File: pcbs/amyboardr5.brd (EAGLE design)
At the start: 106.1 x 47.5 mm, 144 parts, among them J1 52601-G10-8LF, Q2 S8050, Q5 S8050, U1 PCM9211PT, U15 H11L1SR2M, U16 SPX3819, U2 ESP32­S2­SOLO, U3 SPX3819, U4 TL074CD, U6 HX3608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

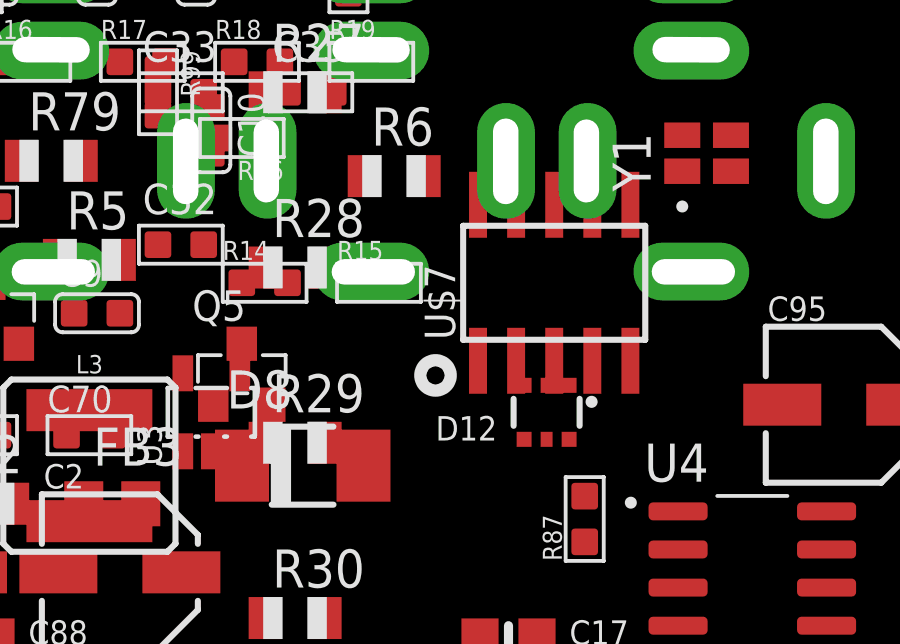
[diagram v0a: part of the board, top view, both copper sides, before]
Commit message: CVOUT fixes
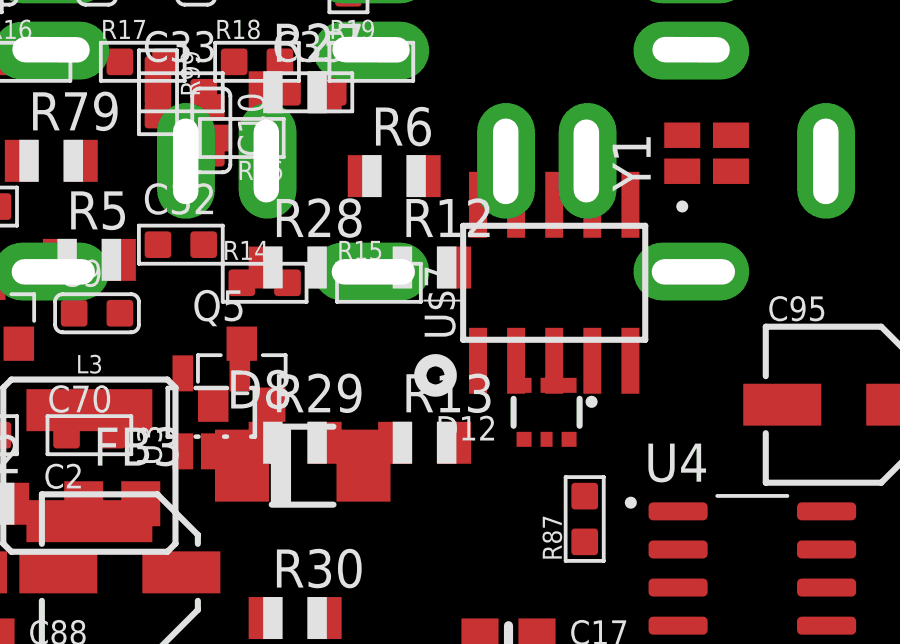
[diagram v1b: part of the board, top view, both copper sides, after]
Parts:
- added R12, R13: 10K, adafruit:R0805
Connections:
- net +3V3: now also R12.1, R13.1
- net N$31: now also R13.2
- net N$33: now also R12.2
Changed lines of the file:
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@@
 <attribute name="VALUE" x="39.116" y="31.1785" size="1.016" layer="27" ratio="12"/>
+</element>
+<element name="R12" library="adafruit" package="R0805" value="10K" x="44.196" y="27.178" smashed="yes">
+<attribute name="NAME" x="43.434" y="28.194" size="1.27" layer="25"/>
+<attribute name="VALUE" x="43.434" y="24.892" size="1.27" layer="27"/>
+</element>
+<element name="R13" library="adafruit" package="R0805" value="10K" x="44.196" y="21.336" smashed="yes">
+<attribute name="NAME" x="43.434" y="22.352" size="1.27" layer="25"/>
+<attribute name="VALUE" x="43.434" y="19.05" size="1.27" layer="27"/>
 </element>
 </elements>
@@
 <contactref element="C107" pad="1"/>
 <contactref element="U16" pad="5"/>
-<wire x1="4.572" y1="35.306" x2="32.02" y2="27.432" width="0" layer="19" extent="1-1"/>
-<wire x1="3.81" y1="25.974" x2="4.572" y2="35.306" width="0" layer="19" extent="1-1"/>
-<wire x1="9.144" y1="20.132" x2="3.81" y2="25.974" width="0" layer="19" extent="1-1"/>
+<contactref element="R12" pad="1"/>
+<contactref element="R13" pad="1"/>
+<wire x1="95.62" y1="43.152" x2="101.026" y2="42.926" width="0" layer="19" extent="1-1"/>
+<wire x1="95.62" y1="44.152" x2="95.62" y2="43.152" width="0" layer="19" extent="1-1"/>
+<wire x1="91.69" y1="45.582" x2="95.62" y2="44.152" width="0" layer="19" extent="1-1"/>
+<wire x1="93.19" y1="37.222" x2="95.62" y2="43.152" width="0" layer="19" extent="1-1"/>
+<wire x1="93.98" y1="26.67" x2="93.19" y2="37.222" width="0" layer="19" extent="1-1"/>
+<wire x1="99.38" y1="28.2241" x2="93.98" y2="26.67" width="0" layer="19" extent="1-1"/>
+<wire x1="106.172" y1="23.876" x2="99.38" y2="28.2241" width="0" layer="19" extent="1-1"/>
+<wire x1="101.6" y1="19.304" x2="106.172" y2="23.876" width="0" layer="19" extent="1-1"/>
+<wire x1="96.604" y1="14.478" x2="101.6" y2="19.304" width="0" layer="19" extent="1-1"/>
+<wire x1="94.506" y1="16.256" x2="96.604" y2="14.478" width="0" layer="19" extent="1-1"/>
+<wire x1="86.106" y1="3.81" x2="96.604" y2="14.478" width="0" layer="19" extent="1-1"/>
+<wire x1="81.026" y1="6.35" x2="86.106" y2="3.81" width="0" layer="19" extent="1-1"/>
+<wire x1="69.215" y1="5.801" x2="81.026" y2="6.35" width="0" layer="19" extent="1-1"/>
+<wire x1="69.215" y1="7.750996875" x2="69.215" y2="5.801" width="0" layer="19" extent="1-1"/>
+<wire x1="63.373" y1="7.751" x2="69.215" y2="7.750996875" width="0" layer="19" extent="1-1"/>
+<wire x1="63.373" y1="3.201003125" x2="63.373" y2="7.751" width="0" layer="19" extent="1-1"/>
+<wire x1="71.392" y1="16.256" x2="69.215" y2="7.750996875" width="0" layer="19" extent="1-1"/>
+<wire x1="74.422" y1="21.082" x2="71.392" y2="16.256" width="0" layer="19" extent="1-1"/>
+<wire x1="67.582" y1="22.606" x2="74.422" y2="21.082" width="0" layer="19" extent="1-1"/>
+<wire x1="60.216" y1="22.606" x2="67.582" y2="22.606" width="0" layer="19" extent="1-1"/>
+<wire x1="61.214" y1="30.988" x2="60.216" y2="22.606" width="0" layer="19" extent="1-1"/>
+<wire x1="49.53" y1="18.034" x2="60.216" y2="22.606" width="0" layer="19" extent="1-1"/>
+<wire x1="47.51" y1="21.452" x2="49.53" y2="18.034" width="0" layer="19" extent="1-1"/>
+<wire x1="66.434" y1="41.582" x2="61.214" y2="30.988" width="0" layer="19" extent="1-1"/>
+<wire x1="37.338" y1="31.496" x2="47.51" y2="21.452" width="0" layer="19" extent="1-1"/>
+<wire x1="35.306" y1="32.258" x2="37.338" y2="31.496" width="0" layer="19" extent="1-1"/>
+<wire x1="32.02" y1="27.432" x2="35.306" y2="32.258" width="0" layer="19" extent="1-1"/>
+<wire x1="41.656" y1="36.322" x2="37.338" y2="31.496" width="0" layer="19" extent="1-1"/>
+<wire x1="38.608" y1="40.132" x2="41.656" y2="36.322" width="0" layer="19" extent="1-1"/>
+<wire x1="25.4" y1="23.434" x2="32.02" y2="27.432" width="0" layer="19" extent="1-1"/>
+<wire x1="21.1" y1="22.098" x2="25.4" y2="23.434" width="0" layer="19" extent="1-1"/>
+<wire x1="29.906" y1="14.732" x2="25.4" y2="23.434" width="0" layer="19" extent="1-1"/>
+<wire x1="30.988" y1="10.922" x2="29.906" y2="14.732" width="0" layer="19" extent="1-1"/>
+<wire x1="10.43" y1="23.876" x2="21.1" y2="22.098" width="0" layer="19" extent="1-1"/>
+<wire x1="9.144" y1="20.132" x2="10.43" y2="23.876" width="0" layer="19" extent="1-1"/>
 <wire x1="9.398" y1="15.936" x2="9.144" y2="20.132" width="0" layer="19" extent="1-1"/>
 <wire x1="12.7" y1="13.97" x2="9.398" y2="15.936" width="0" layer="19" extent="1-1"/>
-<wire x1="30.988" y1="10.922" x2="12.7" y2="13.97" width="0" layer="19" extent="1-1"/>
+<wire x1="3.81" y1="25.974" x2="10.43" y2="23.876" width="0" layer="19" extent="1-1"/>
 <wire x1="3.71" y1="9.636" x2="9.398" y2="15.936" width="0" layer="19" extent="1-16"/>
-<wire x1="21.1" y1="22.098" x2="30.988" y2="10.922" width="0" layer="19" extent="1-1"/>
-<wire x1="25.4" y1="23.434" x2="21.1" y2="22.098" width="0" layer="19" extent="1-1"/>
-<wire x1="29.906" y1="14.732" x2="25.4" y2="23.434" width="0" layer="19" extent="1-1"/>
-<wire x1="35.306" y1="32.258" x2="25.4" y2="23.434" width="0" layer="19" extent="1-1"/>
-<wire x1="37.338" y1="31.496" x2="35.306" y2="32.258" width="0" layer="19" extent="1-1"/>
-<wire x1="41.656" y1="36.322" x2="37.338" y2="31.496" width="0" layer="19" extent="1-1"/>
-<wire x1="38.608" y1="40.132" x2="41.656" y2="36.322" width="0" layer="19" extent="1-1"/>
-<wire x1="47.51" y1="21.452" x2="37.338" y2="31.496" width="0" layer="19" extent="1-1"/>
-<wire x1="49.53" y1="18.034" x2="47.51" y2="21.452" width="0" layer="19" extent="1-1"/>
-<wire x1="60.216" y1="22.606" x2="49.53" y2="18.034" width="0" layer="19" extent="1-1"/>
-<wire x1="67.582" y1="22.606" x2="60.216" y2="22.606" width="0" layer="19" extent="1-1"/>
-<wire x1="74.422" y1="21.082" x2="67.582" y2="22.606" width="0" layer="19" extent="1-1"/>
-<wire x1="71.392" y1="16.256" x2="74.422" y2="21.082" width="0" layer="19" extent="1-1"/>
-<wire x1="61.214" y1="30.988" x2="60.216" y2="22.606" width="0" layer="19" extent="1-1"/>
-<wire x1="69.215" y1="7.750996875" x2="71.392" y2="16.256" width="0" layer="19" extent="1-1"/>
-<wire x1="69.215" y1="5.801" x2="69.215" y2="7.750996875" width="0" layer="19" extent="1-1"/>
-<wire x1="63.373" y1="7.751" x2="69.215" y2="7.750996875" width="0" layer="19" extent="1-1"/>
-<wire x1="63.373" y1="3.201003125" x2="63.373" y2="7.751" width="0" layer="19" extent="1-1"/>
-<wire x1="66.434" y1="41.582" x2="61.214" y2="30.988" width="0" layer="19" extent="1-1"/>
-<wire x1="81.026" y1="6.35" x2="69.215" y2="5.801" width="0" layer="19" extent="1-1"/>
-<wire x1="86.106" y1="3.81" x2="81.026" y2="6.35" width="0" layer="19" extent="1-1"/>
-<wire x1="96.604" y1="14.478" x2="86.106" y2="3.81" width="0" layer="19" extent="1-1"/>
-<wire x1="94.506" y1="16.256" x2="96.604" y2="14.478" width="0" layer="19" extent="1-1"/>
-<wire x1="101.6" y1="19.304" x2="96.604" y2="14.478" width="0" layer="19" extent="1-1"/>
-<wire x1="106.172" y1="23.876" x2="101.6" y2="19.304" width="0" layer="19" extent="1-1"/>
-<wire x1="99.38" y1="28.2241" x2="106.172" y2="23.876" width="0" layer="19" extent="1-1"/>
-<wire x1="93.98" y1="26.67" x2="99.38" y2="28.2241" width="0" layer="19" extent="1-1"/>
-<wire x1="93.19" y1="37.222" x2="93.98" y2="26.67" width="0" layer="19" extent="1-1"/>
-<wire x1="95.62" y1="43.152" x2="93.19" y2="37.222" width="0" layer="19" extent="1-1"/>
-<wire x1="95.62" y1="44.152" x2="95.62" y2="43.152" width="0" layer="19" extent="1-1"/>
-<wire x1="91.69" y1="45.582" x2="95.62" y2="44.152" width="0" layer="19" extent="1-1"/>
-<wire x1="101.026" y1="42.926" x2="95.62" y2="43.152" width="0" layer="19" extent="1-1"/>
-<wire x1="10.43" y1="23.876" x2="32.02" y2="27.432" width="0" layer="19" extent="1-1"/>
+<wire x1="4.572" y1="35.306" x2="3.81" y2="25.974" width="0" layer="19" extent="1-1"/>
+<wire x1="43.196" y1="21.336" x2="101.026" y2="42.926" width="0" layer="19" extent="1-1"/>
+<wire x1="43.196" y1="27.178" x2="43.196" y2="21.336" width="0" layer="19" extent="1-1"/>
 </signal>
 <signal name="DTR">
@@
 <contactref element="R11" pad="1"/>
 <contactref element="U4" pad="6"/>
-<wire x1="4.08" y1="16.256" x2="52.643" y2="12.7" width="0" layer="19" extent="1-1"/>
-<wire x1="4.08" y1="10.414" x2="4.08" y2="16.256" width="0" layer="19" extent="1-1"/>
+<contactref element="R13" pad="2"/>
+<wire x1="52.643" y1="12.7" x2="45.196" y2="21.336" width="0" layer="19" extent="1-1"/>
+<wire x1="4.08" y1="10.414" x2="52.643" y2="12.7" width="0" layer="19" extent="1-1"/>
+<wire x1="4.08" y1="16.256" x2="4.08" y2="10.414" width="0" layer="19" extent="1-1"/>
 </signal>
 <signal name="N$33">
 <contactref element="R22" pad="1"/>
 <contactref element="U4" pad="2"/>
+<contactref element="R12" pad="2"/>
+<wire x1="52.643" y1="17.78" x2="45.196" y2="27.178" width="0" layer="19" extent="1-1"/>
 <wire x1="4.08" y1="4.572" x2="52.643" y2="17.78" width="0" layer="19" extent="1-1"/>
 </signal>

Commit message: dans fixes
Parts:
- R5: value 10K -> 30K
- R6: value 15K -> 10K
- R8: value 30K -> 15K
- moved C10 324.9 mm to (-284.7, 76.5)
- moved R6 324.5 mm to (-278.6, 72.1)
- moved CV_IN1 324.0 mm to (-280.7, 64.3), flipped to the top, turned to 0 degrees
- moved R5 319.9 mm to (-283.7, 72.1)
- moved R8 288.6 mm to (-273.6, 72.1)
- renumbered J1 to MODULAR_PSU
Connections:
- removed net N$17 (its old number): CV_IN1.LEFT/TIP, R8.1
- new net N$16: C9.1, R21.2
- new net N$19: CV_IN1.LEFT/TIP, R5.1
- new net N$23: C10.1, R8.2
- net +3V3: now also R6.1; no longer R5.1
- net 12V: now also C32.1, U3.1, U3.3
- net ADC1: now also R6.2, R8.1; no longer C10.1, R6.1, R8.2
- net ADC2: no longer C9.1
- net GND: now also CV_IN2.GND, U1.35; no longer R21.2, R6.2
- net VPWR: no longer C32.1, U3.1, U3.3

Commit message: ADC cap in parallel
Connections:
- removed net N$16: C9.1, R21.2
- removed net N$23: C10.1, R8.2
- net ADC1: now also C10.1
- net ADC2: now also C9.1
- net GND: now also R21.2, R8.2
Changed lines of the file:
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@@
 <contactref element="C18" pad="2"/>
 <contactref element="C19" pad="2"/>
-<contactref element="C9" pad="2"/>
 <contactref element="MODULAR_PSU" pad="03"/>
 <contactref element="MODULAR_PSU" pad="04"/>
@@
 <contactref element="CV_IN1" pad="GND"/>
 <contactref element="C10" pad="2"/>
-<wire x1="-284.734" y1="75.692" x2="-276.980334375" y2="64.262" width="0" layer="19" extent="1-1"/>
-<wire x1="4.826" y1="38.608" x2="-276.980334375" y2="64.262" width="0" layer="19" extent="1-1"/>
+<contactref element="R8" pad="2"/>
+<contactref element="C9" pad="2"/>
+<contactref element="R21" pad="2"/>
+<wire x1="-272.558" y1="72.136" x2="-276.980334375" y2="64.262" width="0" layer="19" extent="1-1"/>
+<wire x1="-284.734" y1="75.692" x2="-272.558" y2="72.136" width="0" layer="19" extent="1-1"/>
+<wire x1="4.826" y1="38.608" x2="-272.558" y2="72.136" width="0" layer="19" extent="1-1"/>
 <wire x1="6.096" y1="35.306" x2="4.826" y2="38.608" width="0" layer="19" extent="1-1"/>
 <wire x1="6.858" y1="35.052" x2="6.096" y2="35.306" width="0" layer="19" extent="1-1"/>
@@
 <wire x1="5.522" y1="20.574" x2="5.522" y2="23.114" width="0" layer="19" extent="1-1"/>
 <wire x1="9.144" y1="22.032" x2="5.522" y2="23.114" width="0" layer="19" extent="1-1"/>
+<wire x1="5.572" y1="16.002" x2="5.522" y2="20.574" width="0" layer="19" extent="1-1"/>
+<wire x1="3.71" y1="11.636" x2="5.572" y2="16.002" width="0" layer="19" extent="1-16"/>
+<wire x1="11.21" y1="14.036" x2="5.572" y2="16.002" width="0" layer="19" extent="1-16"/>
+<wire x1="12.7" y1="15.494" x2="11.21" y2="14.036" width="0" layer="19" extent="1-16"/>
 <wire x1="11.938" y1="41.91" x2="10.16" y2="35.052" width="0" layer="19" extent="1-1"/>
 <wire x1="13.469" y1="41.91" x2="11.938" y2="41.91" width="0" layer="19" extent="1-1"/>
-<wire x1="12.7" y1="15.494" x2="9.144" y2="22.032" width="0" layer="19" extent="1-1"/>
-<wire x1="11.21" y1="14.036" x2="12.7" y2="15.494" width="0" layer="19" extent="1-16"/>
-<wire x1="3.71" y1="11.636" x2="11.21" y2="14.036" width="0" layer="19" extent="16-16"/>
 <wire x1="19.606" y1="10.26" x2="12.7" y2="15.494" width="0" layer="19" extent="1-1"/>
 <wire x1="17.206" y1="2.76" x2="19.606" y2="10.26" width="0" layer="19" extent="1-1"/>
@@
 <contactref element="R6" pad="2"/>
 <contactref element="R5" pad="2"/>
+<contactref element="C10" pad="1"/>
 <wire x1="-277.638" y1="72.136" x2="-282.718" y2="72.136" width="0" layer="19" extent="1-1"/>
 <wire x1="-274.558" y1="72.136" x2="-277.638" y2="72.136" width="0" layer="19" extent="1-1"/>
+<wire x1="-284.734" y1="77.216" x2="-282.718" y2="72.136" width="0" layer="19" extent="1-1"/>
 <wire x1="66.434" y1="32.692" x2="-274.558" y2="72.136" width="0" layer="19" extent="1-1"/>
 </signal>
@@
 <contactref element="R21" pad="1"/>
 <contactref element="R7" pad="2"/>
-<wire x1="12.43" y1="23.876" x2="91.678" y2="24.892" width="0" layer="19" extent="1-1"/>
+<contactref element="C9" pad="1"/>
+<wire x1="32.512" y1="25.654" x2="91.678" y2="24.892" width="0" layer="19" extent="1-1"/>
+<wire x1="12.43" y1="23.876" x2="32.512" y2="25.654" width="0" layer="19" extent="1-1"/>
 <wire x1="3.572" y1="16.002" x2="12.43" y2="23.876" width="0" layer="19" extent="1-1"/>
 </signal>
@@
 <wire x1="38.034" y1="23.6521" x2="39.624" y2="33.02" width="0" layer="19" extent="1-1"/>
 </signal>
-<signal name="N$16">
-<contactref element="R21" pad="2"/>
-<contactref element="C9" pad="1"/>
-<wire x1="5.572" y1="16.002" x2="32.512" y2="25.654" width="0" layer="19" extent="1-1"/>
-</signal>
 <signal name="N$17">
 <contactref element="CV_IN1" pad="RIGHT/RING"/>
 </signal>
-<signal name="N$23">
-<contactref element="R8" pad="2"/>
-<contactref element="C10" pad="1"/>
-<wire x1="-272.558" y1="72.136" x2="-284.734" y2="77.216" width="0" layer="19" extent="1-1"/>
-</signal>
 <signal name="N$13">

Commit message: moving parts
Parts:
- moved CV_IN1 324.0 mm to (42.4, 40.6), flipped to the bottom, turned to 270 degrees
- moved R5 320.1 mm to (34.5, 37.6), turned to 90 degrees
- moved C10 317.5 mm to (30.2, 36.6), turned to 90 degrees
- moved R6 314.6 mm to (34.5, 42.7), turned to 90 degrees
- moved R8 309.1 mm to (34.5, 47.8), turned to 90 degrees
- flipped 1-10VPP to the top
